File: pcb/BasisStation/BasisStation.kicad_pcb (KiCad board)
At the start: 2 copper layers, 160 x 135 mm, 22 parts, among them J1 Conn_02x05_Odd_Even, J2 Conn_02x03_Odd_Even, U1 ESP32-S3-WROOM-1

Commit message: v0.00.001 fix(SHBS-7): U6 auf ESP32-S3-WROOM-1U-N16R8-Symbol umgestellt
Espressif-Stil-Symbol in Bauteile-Bibliothek, sym-lib-table ergänzt.
Schaltplan, Netlist und PCB-Value für U6 auf N16R8 vereinheitlicht.
ERC ohne Fehler (ERC.rpt aktualisiert).

Co-authored-by: Cursor <cursoragent@cursor.com>
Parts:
- U6: renamed from U1; value ESP32-S3-WROOM-1 -> ESP32-S3-WROOM-1U-N16R8

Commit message: v0.00.001 feat(SHBS-4): USB-C-Stromversorgung mit MP2359-Buck auf 3,3V
PS2/+12V entfernt, neue Stromversorgungs-Schaltung (Stromversorgung.kicad_sch),
Footprints fuer MP2359DJ, SOT-23-6 und USB-C-Buchse, power_supply.md als
zentrale Referenz.

Co-Authored-By: Claude Sonnet 5 <noreply@anthropic.com>
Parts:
- removed PS1: TSR_1-2433E, Footprints:CONV_TSR_1-2433E

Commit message: v0.00.001 refactor(SHBS-12): KiCad-Bibliotheken auf Bauteilordner umgestellt
Symbol, Footprint und 3D-Modell eines Bauteils lagen bisher in drei
getrennten Sammelordnern. Jedes Bauteil hat jetzt einen eigenen Ordner
unter pcb/Bauteile/; pcb/Symbol/, pcb/Footprints/ und pcb/3D-Model/
entfallen.

Umfang: 20 Dateien verschoben, 13 verwaiste entfernt, 63 Footprint-
Referenzen in Schaltplaenen, Netzliste und Board umgeschrieben, 7
Footprint-Vorgaben in den Symbol-Dateien angepasst.

Nebenbei behoben:
- Die 3D-Modelle waren im Board ueber absolute Pfade auf E: und in der
  Netzliste auf C: verdrahtet, funktionsfaehig jeweils nur auf einem
  Rechner. Jetzt durchgaengig ueber ${KIPRJMOD}.
- Drei Footprint-Referenzen zeigten auf Bibliotheken, die nie in der
  fp-lib-table standen.
- WCAP-FTXX_P10 hatte keine Footprint-Vorgabe, der W5500-Footprint keine
  3D-Referenz.
- fp-info-cache und *.kicad_prl sind nicht mehr versioniert.

Verifikation: Projekt oeffnet ohne Bibliotheks-Warnung. ERC 0 Fehler und
7 Warnungen, vorher 9, keine neue. DRC meldet "Found 0 Footprint errors";
der verbliebene DRC-Fehler ist eine vorbestehende Routing-Luecke im
EN-Netz. 3D-Ansicht zeigt die Modelle.

Co-Authored-By: Claude Opus 5 <noreply@anthropic.com>
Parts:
- C1, C4, C5: footprint Footprints:WCAP-FTXX_P10L13W7H13 -> WCAP-FTXX_P10:WCAP-FTXX_P10L13W7H13
- C3: footprint Footprints:WCAP-PT5H_6.3X5.2_DXL_ -> WCAP-PT5H_6.3X5.2:WCAP-PT5H_6.3X5.2_DXL_
- D1, D2: footprint Footprints:WL-TMRW_3MM -> WL-TMRW_3MM:WL-TMRW_3MM
- D4, D5: footprint Footprints:WL-TMRC_3MM -> WL-TMRC_3MM:WL-TMRC_3MM
- J1: footprint Footprints:61201021621 -> wuerth_6120XX21621:61201021621
- J2: footprint Footprints:61200621621 -> wuerth_6120XX21621:61200621621
- S1: footprint Footprints:1543650149 -> 1543-650-149:1543650149
- U6: footprint Footprints:ESP32-S3-WROOM-1U -> ESP32-S3-WROOM-1U-N16R8:ESP32-S3-WROOM-1U
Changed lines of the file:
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@@
 		(embedded_fonts no)
 	)
-	(footprint "Footprints:61201021621"
+	(footprint "wuerth_6120XX21621:61201021621"
 		(layer "F.Cu")
 		(at 197.27 103.58 90)
@@
 		)
 		(embedded_fonts no)
-		(model "E:/Projekte/SmartHomeSystemBasisStation/pcb/3D-Model/6120XX21621_61201021621.step"
+		(model "${KIPRJMOD}/../Bauteile/wuerth_6120XX21621/6120XX21621_61201021621.step"
 			(offset
 				(xyz 0 0 4.5)
@@
 		)
 	)
-	(footprint "Footprints:WL-TMRC_3MM"
+	(footprint "WL-TMRC_3MM:WL-TMRC_3MM"
 		(layer "F.Cu")
 		(at 109.5 153.5)
@@
 		)
 		(embedded_fonts no)
-		(model "E:/Projekte/SmartHomeSystemBasisStation/pcb/3D-Model/WL-TMRC_3MM.step"
+		(model "${KIPRJMOD}/../Bauteile/WL-TMRC_3MM/WL-TMRC_3MM.step"
 			(offset
 				(xyz 0 0 5)
@@
 		(embedded_fonts no)
 	)
-	(footprint "Footprints:1543650149"
+	(footprint "1543-650-149:1543650149"
 		(layer "F.Cu")
 		(at 177.5 32.5 180)
@@
 		(embedded_fonts no)
 	)
-	(footprint "Footprints:WCAP-FTXX_P10L13W7H13"
+	(footprint "WCAP-FTXX_P10:WCAP-FTXX_P10L13W7H13"
 		(layer "F.Cu")
 		(at 187.5 54 180)
@@
 		)
 		(embedded_fonts no)
-		(model "E:/Projekte/SmartHomeSystemBasisStation/pcb/3D-Model/WCAP-FTXX_P10.step"
+		(model "${KIPRJMOD}/../Bauteile/WCAP-FTXX_P10/WCAP-FTXX_P10.step"
 			(offset
 				(xyz 0 0 6)
@@
 		)
 	)
-	(footprint "Footprints:WL-TMRW_3MM"
+	(footprint "WL-TMRW_3MM:WL-TMRW_3MM"
 		(layer "F.Cu")
 		(at 128.5 153.5)
@@
 		)
 		(embedded_fonts no)
-		(model "E:/Projekte/SmartHomeSystemBasisStation/pcb/3D-Model/WL-TMRW_3MM.step"
+		(model "${KIPRJMOD}/../Bauteile/WL-TMRW_3MM/WL-TMRW_3MM.step"
 			(offset
 				(xyz 0 0 4.5)
@@
 		)
 	)
-	(footprint "Footprints:WCAP-FTXX_P10L13W7H13"
+	(footprint "WCAP-FTXX_P10:WCAP-FTXX_P10L13W7H13"
 		(layer "F.Cu")
 		(at 126 65)
@@
 		)
 		(embedded_fonts no)
-		(model "E:/Projekte/SmartHomeSystemBasisStation/pcb/3D-Model/WCAP-FTXX_P10.step"
+		(model "${KIPRJMOD}/../Bauteile/WCAP-FTXX_P10/WCAP-FTXX_P10.step"
 			(offset
 				(xyz 0 0 6)
@@
 		)
 	)
-	(footprint "Footprints:WCAP-PT5H_6.3X5.2_DXL_"
+	(footprint "WCAP-PT5H_6.3X5.2:WCAP-PT5H_6.3X5.2_DXL_"
 		(layer "F.Cu")
 		(at 102.5 44.75 90)
@@
 		(embedded_fonts no)
 	)
-	(footprint "Footprints:WCAP-FTXX_P10L13W7H13"
+	(footprint "WCAP-FTXX_P10:WCAP-FTXX_P10L13W7H13"
 		(layer "F.Cu")
 		(at 163 42 -90)
@@
 		)
 		(embedded_fonts no)
-		(model "E:/Projekte/SmartHomeSystemBasisStation/pcb/3D-Model/WCAP-FTXX_P10.step"
+		(model "${KIPRJMOD}/../Bauteile/WCAP-FTXX_P10/WCAP-FTXX_P10.step"
 			(offset
 				(xyz 0 0 6)
@@
 		)
 	)
-	(footprint "Footprints:ESP32-S3-WROOM-1U"
+	(footprint "ESP32-S3-WROOM-1U-N16R8:ESP32-S3-WROOM-1U"
 		(layer "F.Cu")
 		(at 135.985 86)
@@
 		)
 		(embedded_fonts no)
-		(model "E:/Projekte/SmartHomeSystemBasisStation/pcb/3D-Model/ESP32-S3-WROOM-1U.STEP"
+		(model "${KIPRJMOD}/../Bauteile/ESP32-S3-WROOM-1U-N16R8/ESP32-S3-WROOM-1U.STEP"
 			(offset
 				(xyz -9 -9.8 0)
@@
 		)
 	)
-	(footprint "Footprints:WL-TMRW_3MM"
+	(footprint "WL-TMRW_3MM:WL-TMRW_3MM"
 		(layer "F.Cu")
 		(at 119 153.5)
@@
 		)
 		(embedded_fonts no)
-		(model "E:/Projekte/SmartHomeSystemBasisStation/pcb/3D-Model/WL-TMRW_3MM.step"
+		(model "${KIPRJMOD}/../Bauteile/WL-TMRW_3MM/WL-TMRW_3MM.step"
 			(offset
 				(xyz 0 0 4.5)
@@
 		)
 	)
-	(footprint "Footprints:61200621621"
+	(footprint "wuerth_6120XX21621:61200621621"
 		(layer "F.Cu")
 		(at 197.23 78.04 -90)
@@
 		)
 		(embedded_fonts no)
-		(model "E:/Projekte/SmartHomeSystemBasisStation/pcb/3D-Model/6120XX21621_61200621621.step"
+		(model "${KIPRJMOD}/../Bauteile/wuerth_6120XX21621/6120XX21621_61200621621.step"
 			(offset
 				(xyz 0 0 4.5)
@@
 		)
 	)
-	(footprint "Footprints:WL-TMRC_3MM"
+	(footprint "WL-TMRC_3MM:WL-TMRC_3MM"
 		(layer "F.Cu")
 		(at 138 153.5)
@@
 		)
 		(embedded_fonts no)
-		(model "E:/Projekte/SmartHomeSystemBasisStation/pcb/3D-Model/WL-TMRC_3MM.step"
+		(model "${KIPRJMOD}/../Bauteile/WL-TMRC_3MM/WL-TMRC_3MM.step"
 			(offset
 				(xyz 0 0 5)

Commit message: v0.00.001 (WIP) feat(SHBS-21): Stromversorgung und Status-LEDs im PCB platziert und geroutet
Erster Layout-Stand von Stromversorgung und LEDs inkl. Anbindung der
USB-C-Pads B4/B9/A12/B12 (SHBS-20), Zonen neu gefüllt. ethernet.kicad_sch
enthält nur eine von KiCad neu geschriebene Symbolkopie. PCB-Review als
Report abgelegt.

Co-Authored-By: Claude Opus 5.5 <noreply@anthropic.com>
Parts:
- removed C1, C4, C5: WCAP-FTXX_P10, WCAP-FTXX_P10:WCAP-FTXX_P10L13W7H13
- removed C3: WCAP-PT5H_6.3X5.2, WCAP-PT5H_6.3X5.2:WCAP-PT5H_6.3X5.2_DXL_
- removed D1: RED, WL-TMRW_3MM:WL-TMRW_3MM
- removed D2: BLUE, WL-TMRW_3MM:WL-TMRW_3MM
- removed D4: GREEN, WL-TMRC_3MM:WL-TMRC_3MM
- removed D5: YELLOW, WL-TMRC_3MM:WL-TMRC_3MM
- removed J2: Conn_02x03_Odd_Even, wuerth_6120XX21621:61200621621
- removed R1: 0, Resistor_THT:R_Axial_DIN0207_L6.3mm_D2.5mm_P10.16mm_Horizontal
- removed R2, R3, R4, R5: 220, Resistor_THT:R_Axial_DIN0617_L17.0mm_D6.0mm_P20.32mm_Horizontal
- removed S1: 1543-650-149, 1543-650-149:1543650149
- added C10: WCAP-FTXX_P10, WCAP-FTXX_P10:WCAP-FTXX_P10L13W7H13, F.Cu at (-21.5, 80.8)
- added C12: WCAP-FTXX_P10, WCAP-FTXX_P10:WCAP-FTXX_P10L13W7H13, F.Cu at (-21.5, 89.5)
- added C13: 10uF, Capacitor_SMD:C_0805_2012Metric, F.Cu at (56.5, 48.5)
- added C14: 22uF, Capacitor_SMD:C_0805_2012Metric, F.Cu at (75.5, 66.5)
- added C15: 100 nF, Capacitor_SMD:C_0805_2012Metric, F.Cu at (57.0, 54.0)
- added C16: 100nF, Capacitor_SMD:C_0805_2012Metric, F.Cu at (9.03, 70.4)
- added C17: 100nF, Capacitor_SMD:C_0805_2012Metric, F.Cu at (9.03, 73.4)
- added C18: 100nF, Capacitor_SMD:C_0805_2012Metric, F.Cu at (9.03, 76.4)
- added C19: 100nF, Capacitor_SMD:C_0805_2012Metric, F.Cu at (9.03, 79.4)
- added C20: 100nF, Capacitor_SMD:C_0805_2012Metric, F.Cu at (13.5, 70.4)
- added C21: 100nF, Capacitor_SMD:C_0805_2012Metric, F.Cu at (13.5, 73.4)
- added C22: 100nF, Capacitor_SMD:C_0805_2012Metric, F.Cu at (13.5, 76.4)
- added C23: 4,7 µF, Capacitor_SMD:C_0805_2012Metric, F.Cu at (13.5, 79.4)
- added C24: 10nF, Capacitor_SMD:C_0805_2012Metric, F.Cu at (17.9, 70.4)
- added C25: 27 pF, Capacitor_SMD:C_0805_2012Metric, F.Cu at (17.9, 73.4)
- added C26: 27 pF, Capacitor_SMD:C_0805_2012Metric, F.Cu at (17.9, 76.4)
- added C27: 10 µF, Capacitor_SMD:C_0805_2012Metric, F.Cu at (17.9, 79.4)
- added C28: 1nF/2kV, Capacitor_SMD:C_1206_3216Metric, F.Cu at (34.4, 74.4)
- added C29: 6,8nF, Capacitor_SMD:C_0805_2012Metric, F.Cu at (22.4, 70.4)
- added C30: 6,8nF, Capacitor_SMD:C_0805_2012Metric, F.Cu at (22.4, 73.4)
- added C31: 10nF, Capacitor_SMD:C_0805_2012Metric, F.Cu at (22.4, 76.4)
- added C32: 22nF, Capacitor_SMD:C_0805_2012Metric, F.Cu at (22.4, 79.4)
- added C7: WCAP-FTXX_P10, WCAP-FTXX_P10:WCAP-FTXX_P10L13W7H13, F.Cu at (-21.5, 72.1)
- added C8: WCAP-PT5H_6.3X5.2, WCAP-PT5H_6.3X5.2:WCAP-PT5H_6.3X5.2_DXL_, F.Cu at (-3.60, 83.0)
- added D10: GREEN, WL-TMRC_3MM:WL-TMRC_3MM, F.Cu at (123.7, 155.0)
- added D11: SS34, Diode_SMD:D_SMA, F.Cu at (59.5, 61.5)
- added D12: SMAJ5.0A, Diode_SMD:D_SMA, F.Cu at (58.0, 42.0)
- added D7: YELLOW, WL-TMRC_3MM:WL-TMRC_3MM, F.Cu at (112.0, 155.0)
- added D8: BLUE, WL-TMRW_3MM:WL-TMRW_3MM, F.Cu at (134.7, 155.0)
- added D9: RED, WL-TMRW_3MM:WL-TMRW_3MM, F.Cu at (144.7, 155.0)
- added F1: 1.1A, Fuse:Fuse_1206_3216Metric, F.Cu at (66.0, 43.5)
- added FB1: Ferrit 600R@100MHz, Inductor_SMD:L_0805_2012Metric, F.Cu at (33.9, 77.5)
- added J6: 61200621621, wuerth_6120XX21621:61200621621, F.Cu at (-5.62, 96.3)
- added J_PWR1: 12401598E4-2A, shbs_power:USB_C_Receptacle_Amphenol_12401598E4-2A, F.Cu at (72.5, 31.5)
- added L1: 10uH, Inductor_SMD:L_Bourns_SRN6045TA, F.Cu at (59.5, 70.0)
- added PS1: AP3211, shbs_power:MP2359DJ, F.Cu at (66.0, 53.5)
- added Q1: BC337, Package_TO_SOT_THT:TO-92_Inline, F.Cu at (132.7, 118.0)
- added Q2: BC337, Package_TO_SOT_THT:TO-92_Inline, F.Cu at (121.7, 118.0)
- added Q3: BC337, Package_TO_SOT_THT:TO-92_Inline, F.Cu at (143.2, 118.0)
- added Q4: BC337, Package_TO_SOT_THT:TO-92_Inline, F.Cu at (110.2, 117.9)
- added R13: 220, Resistor_THT:R_Axial_DIN0617_L17.0mm_D6.0mm_P20.32mm_Horizontal, F.Cu at (111.5, 127.2)
- added R14: 220, Resistor_THT:R_Axial_DIN0617_L17.0mm_D6.0mm_P20.32mm_Horizontal, F.Cu at (134.5, 147.7)
- added R15: 220, Resistor_THT:R_Axial_DIN0617_L17.0mm_D6.0mm_P20.32mm_Horizontal, F.Cu at (145.0, 127.2)
- added R16: 220, Resistor_THT:R_Axial_DIN0617_L17.0mm_D6.0mm_P20.32mm_Horizontal, F.Cu at (123.5, 127.3)
- added R17: 49,9 kΩ, Resistor_SMD:R_0805_2012Metric, F.Cu at (73.0, 60.5)
- added R18: 16,2 kΩ, Resistor_SMD:R_0805_2012Metric, F.Cu at (76.5, 55.0)
- added R19: 5,1 kΩ, Resistor_SMD:R_0805_2012Metric, F.Cu at (75.5, 43.4)
- added R20: 5,1 kΩ, Resistor_SMD:R_0805_2012Metric, F.Cu at (71.0, 43.4)
- added R21: 5,1 kΩ, Resistor_SMD:R_0805_2012Metric, F.Cu at (20.8, 109.9)
- added R22: 5,1 kΩ, Resistor_SMD:R_0805_2012Metric, F.Cu at (20.8, 112.9)
- added R23: 4,7k, Resistor_THT:R_Axial_DIN0617_L17.0mm_D6.0mm_P20.32mm_Horizontal, F.Cu at (111.5, 88.8)
- added R24: 4,7k, Resistor_THT:R_Axial_DIN0617_L17.0mm_D6.0mm_P20.32mm_Horizontal, F.Cu at (144.5, 88.7)
- added R25: 4,7k, Resistor_THT:R_Axial_DIN0617_L17.0mm_D6.0mm_P20.32mm_Horizontal, F.Cu at (123.0, 88.8)
- added R26: 4,7k, Resistor_THT:R_Axial_DIN0617_L17.0mm_D6.0mm_P20.32mm_Horizontal, F.Cu at (134.0, 88.8)
- added R27: 12,4kΩ, 1%, Resistor_SMD:R_0805_2012Metric, F.Cu at (28.6, 47.6)
- added R28: 10kΩ, Resistor_SMD:R_0805_2012Metric, F.Cu at (28.6, 50.5)
- added R29: 10kΩ, Resistor_SMD:R_0805_2012Metric, F.Cu at (28.6, 53.5)
- added R30: 10kΩ, Resistor_SMD:R_0805_2012Metric, F.Cu at (28.6, 56.4)
- added R31: 10kΩ, Resistor_SMD:R_0805_2012Metric, F.Cu at (28.6, 59.4)
- added R32: 10kΩ, Resistor_SMD:R_0805_2012Metric, F.Cu at (33.0, 47.6)
- added R33: 220Ω, Resistor_SMD:R_0805_2012Metric, F.Cu at (33.0, 50.5)
- added R34: 220Ω, Resistor_SMD:R_0805_2012Metric, F.Cu at (33.0, 53.5)
- added R35: 0Ω, Resistor_SMD:R_0805_2012Metric, F.Cu at (33.0, 56.4)
- added R36: 49,9Ω 1%, Resistor_SMD:R_0805_2012Metric, F.Cu at (33.0, 59.4)
- added R37: 49,9Ω 1%, Resistor_SMD:R_0805_2012Metric, F.Cu at (37.4, 47.6)
- added R38: 10Ω 1%, Resistor_SMD:R_0805_2012Metric, F.Cu at (37.4, 50.5)
- added R39: 49,9Ω 1%, Resistor_SMD:R_0805_2012Metric, F.Cu at (37.4, 53.5)
- added R40: 49,9Ω 1%, Resistor_SMD:R_0805_2012Metric, F.Cu at (37.4, 56.4)
- added R9: 10k, Resistor_THT:R_Axial_DIN0207_L6.3mm_D2.5mm_P10.16mm_Horizontal, F.Cu at (-12.5, 103.6)
- added S2: 1543-650-149, 1543-650-149:1543650149, F.Cu at (-4.14, 52.6)
- added T1: 7499011121A, wuerth_rj45:T_Wurth_WE-RJ45LAN_7499011121A, F.Cu at (12.2, 50.9)
- added U1: D3V3XA4B10LP, Package_DFN_QFN:Diodes_UDFN-10_1x2.5mm_P0.5mm, F.Cu at (20.1, 116.5)
- added U7: W5500, W5500:48LQFP_W5500_WIZ, F.Cu at (32.3, 66.8)
- added Y1: 25 MHz, wuerth_830059532:Y_Wurth_WE-XTAL_Quartz-CFPX-104, F.Cu at (29.0, 76.3)
- J1: value Conn_02x05_Odd_Even -> 12401598E4-2A; footprint wuerth_6120XX21621:61201021621 -> shbs_power:USB_C_Receptacle_Amphenol_12401598E4-2A
- moved J1 184.9 mm to (12.7, 114.9), turned to 0 degrees
- moved U6 16.6 mm to (128.1, 71.4)
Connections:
- U6 pad 13: unconnected-(U1-GPIO19/U1RTS/ADC2_CH8/CLK_OUT2/USB_D--Pad13) -> USB-
- U6 pad 14: unconnected-(U1-GPIO20/U1CTS/ADC2_CH9/CLK_OUT1/USB_D+-Pad14) -> USB+
- U6 pad 15: Net-(U1-GPIO3/TOUCH3/ADC1_CH2) -> unconnected-(U6-GPIO3/TOUCH3/ADC1_CH2-Pad15)
- U6 pad 16: Net-(U1-GPIO46) -> unconnected-(U6-GPIO46-Pad16)
- U6 pad 17: unconnected-(U1-GPIO9/TOUCH9/ADC1_CH8/FSPIHD/SUBSPIHD-Pad17) -> ETH_RST
- U6 pad 18: unconnected-(U1-GPIO10/TOUCH10/ADC1_CH9/FSPICS0/FSPIIO4/SUBSPICS0-Pad18) -> ETH_SCSn
- U6 pad 19: unconnected-(U1-GPIO11/TOUCH11/ADC2_CH0/FSPID/FSPIIO5/SUBSPID-Pad19) -> ETH_MOSI
- U6 pad 20: unconnected-(U1-GPIO12/TOUCH12/ADC2_CH1/FSPICLK/FSPIIO6/SUBSPICLK-Pad20) -> ETH_SCLK
- U6 pad 21: unconnected-(U1-GPIO13/TOUCH13/ADC2_CH2/FSPIQ/FSPIIO7/SUBSPIQ-Pad21) -> ETH_MISO
- U6 pad 22: unconnected-(U1-GPIO14/TOUCH14/ADC2_CH3/FSPIWP/FSPIDQS/SUBSPIWP-Pad22) -> ETH_INT
- U6 pad 24: unconnected-(U1-GPIO47/SPICLK_P/SUBSPICLK_P_DIFF-Pad24) -> Net-(U6-GPIO47/SPICLK_P/SUBSPICLK_P_DIFF)
- U6 pad 25: unconnected-(U1-GPIO48/SPICLK_N/SUBSPICLK_N_DIFF-Pad25) -> Net-(U6-GPIO48/SPICLK_N/SUBSPICLK_N_DIFF)
- U6 pad 26: Net-(U1-GPIO45) -> unconnected-(U6-GPIO45-Pad26)
- U6 pad 3: EN -> /Layout/EN
- U6 pad 31: unconnected-(U1-GPIO38/FSPIWP/SUBSPIWP-Pad31) -> Net-(U6-GPIO38/FSPIWP/SUBSPIWP)
- U6 pad 32: Net-(J1-Pin_4) -> unconnected-(U6-MTCK/GPIO39/CLK_OUT3/SUBSPICS1-Pad32)
- U6 pad 33: Net-(J1-Pin_6) -> unconnected-(U6-MTDO/GPIO40/CLK_OUT2-Pad33)
- U6 pad 34: Net-(J1-Pin_8) -> unconnected-(U6-MTDI/GPIO41/CLK_OUT1-Pad34)
- U6 pad 35: Net-(J1-Pin_2) -> unconnected-(U6-MTMS/GPIO42-Pad35)
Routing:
- net +3V3: track 650.0 -> 21.5 mm
- net EN: track 109.2 -> 0.00 mm, vias 2 -> 0
- net Net-(J6-Pin_6): track 62.3 -> 0.00 mm, vias 2 -> 0
- net Net-(J1-Pin_2): track 61.4 -> 0.00 mm, vias 2 -> 0
- net Net-(J1-Pin_4): track 58.8 -> 0.00 mm
- net Net-(J1-Pin_6): track 58.3 -> 0.00 mm
- net Net-(J1-Pin_8): track 57.8 -> 0.00 mm
- net Net-(J6-Pin_3): track 52.7 -> 0.00 mm
- net Net-(J6-Pin_5): track 52.2 -> 0.00 mm
- net GND: track 0.00 -> 50.1 mm, vias 0 -> 5
- net Net-(D11-K): track 0.00 -> 40.7 mm
- net Net-(U1-GPIO3/TOUCH3/ADC1_CH2): track 27.1 -> 0.00 mm
- net Net-(J_PWR1-CC2): track 0.00 -> 24.6 mm, vias 0 -> 2
- net Net-(U1-GPIO46): track 21.9 -> 0.00 mm
- net Net-(U6-GPIO38/FSPIWP/SUBSPIWP): track 0.00 -> 21.2 mm
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
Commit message: v0.00.001 (WIP) feat(SHBS-21): Netzklasse Power, Label SW und Session-Übergabe
Netzklasse Power (0,6 mm, Via 0,8/0,4) mit Mustern für VBUS, +5V, SW,
+3V3 und GND. Schaltknoten im Schaltplan als lokales Label SW benannt,
PCB per F8 nachgezogen. power_supply.md ergänzt. tmp/memory.md hält den
Session-Stand für die Weiterarbeit auf einem anderen Rechner fest
(nächster Schritt: Buck-Wandler kompakt platzieren).

Co-Authored-By: Claude Opus 5.5 <noreply@anthropic.com>
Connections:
- net Net-(D11-K) renamed /Stromversorgung/SW
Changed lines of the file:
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@@
 	(net 3 "/Layout/EN")
 	(net 4 "/Stromversorgung/+5V")
-	(net 5 "Net-(D11-K)")
+	(net 5 "/Stromversorgung/SW")
 	(net 6 "Net-(PS1-BST)")
 	(net 7 "/Ethernet/+3V3A")
@@
 			(size 2.35 5.1)
 			(layers "F.Cu" "F.Mask" "F.Paste")
-			(net 5 "Net-(D11-K)")
+			(net 5 "/Stromversorgung/SW")
 			(pinfunction "2")
 			(pintype "passive")
@@
 			(layers "F.Cu" "F.Mask" "F.Paste")
 			(roundrect_rratio 0.25)
-			(net 5 "Net-(D11-K)")
+			(net 5 "/Stromversorgung/SW")
 			(pinfunction "SW")
 			(pintype "output")
@@
 			(layers "F.Cu" "F.Mask" "F.Paste")
 			(roundrect_rratio 0.1388888889)
-			(net 5 "Net-(D11-K)")
+			(net 5 "/Stromversorgung/SW")
 			(pinfunction "K")
 			(pintype "passive")
@@
 			(layers "F.Cu" "F.Mask" "F.Paste")
 			(roundrect_rratio 0.25)
-			(net 5 "Net-(D11-K)")
+			(net 5 "/Stromversorgung/SW")
 			(pintype "passive")
 		)

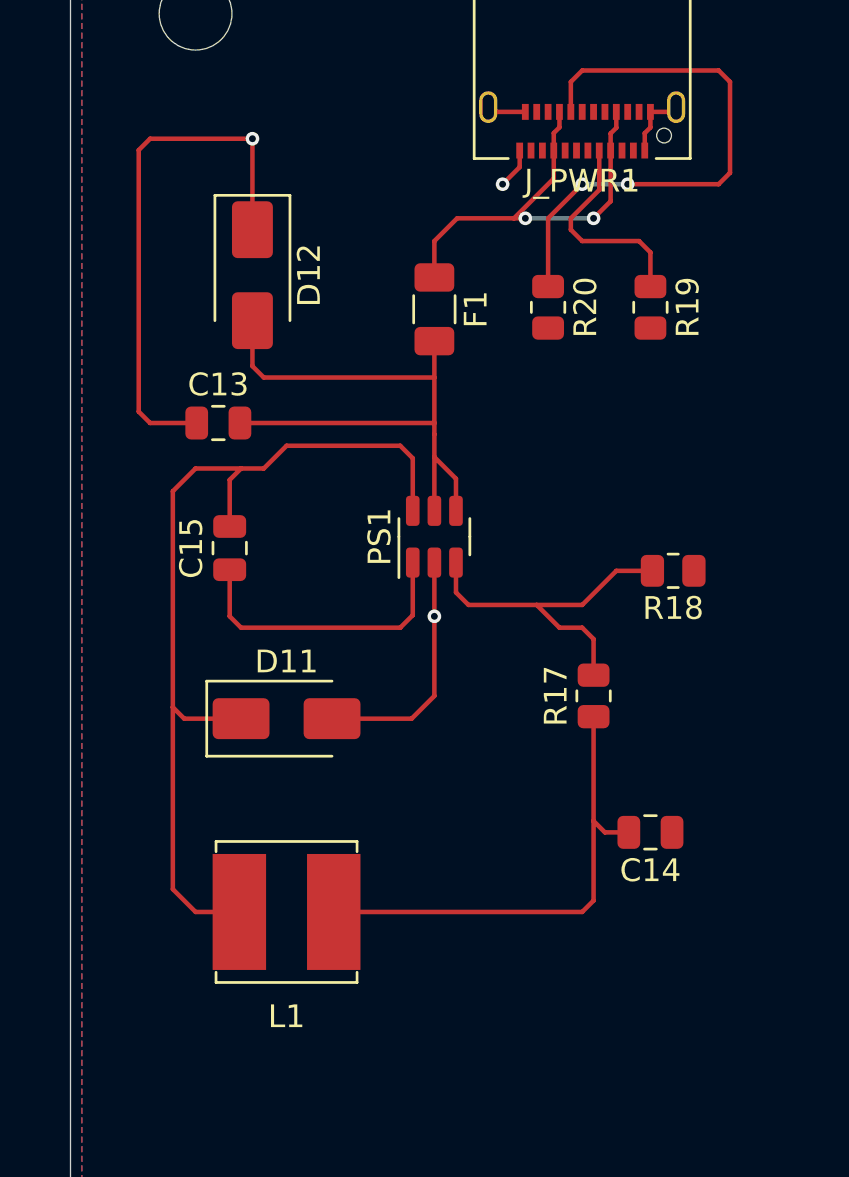
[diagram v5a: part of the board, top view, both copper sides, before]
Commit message: v0.00.001 (WIP) feat(SHBS-21): Buck-Wandler kompakt um PS1 platziert und neu geroutet
C13, C15, D11, L1, C14, R17, R18 eng um PS1 angeordnet, Leitungen am
Wandler neu verlegt (Power 0,6 mm, 5 GND-Vias). SW-Leitung ca. 9,2 mm
statt 40,7 mm. DRC im Wandler-Bereich ohne Befund, offen: +3V3 (B4).

Co-Authored-By: Claude Opus 5.5 <noreply@anthropic.com>
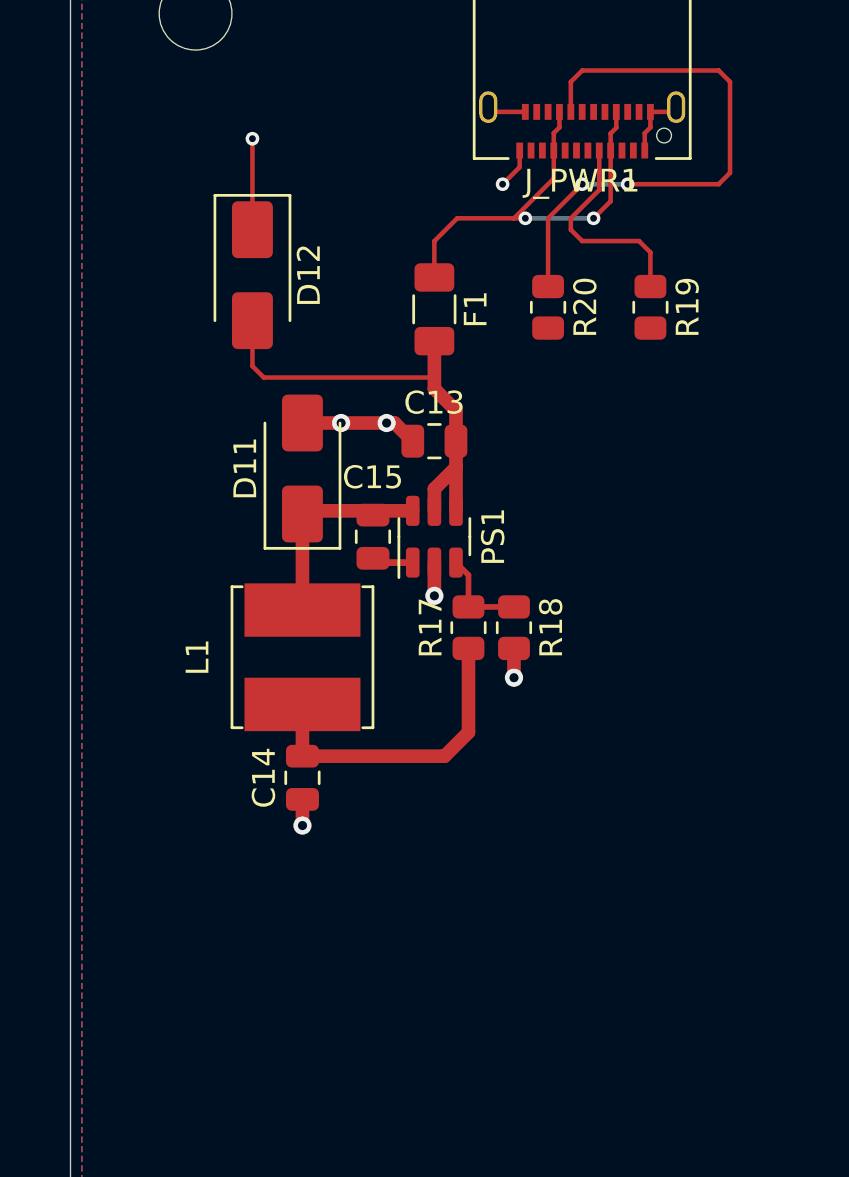
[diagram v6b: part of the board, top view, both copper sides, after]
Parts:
- moved C14 15.5 mm to (60.2, 64.1), turned to 90 degrees
- moved L1 11.2 mm to (60.2, 58.8), turned to 90 degrees
- moved D11 11.0 mm to (60.2, 50.5), turned to 90 degrees
- moved C13 9.53 mm to (66.0, 49.3)
- moved R18 7.43 mm to (69.5, 57.5), turned to 90 degrees
- moved C15 6.32 mm to (63.3, 53.5)
- moved R17 6.26 mm to (67.5, 57.5)
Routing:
- net /Stromversorgung/SW: track 40.7 -> 9.21 mm
- net GND: track 50.1 -> 28.9 mm, vias 5 -> 9
- net Net-(PS1-FB): track 15.5 -> 4.18 mm
- net Net-(PS1-BST): track 12.8 -> 1.75 mm
- net /Stromversorgung/+5V: track 20.8 -> 12.2 mm
- net +3V3: track 21.5 -> 13.7 mm
